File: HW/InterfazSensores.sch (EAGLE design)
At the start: 30 parts, among them IC1 LM2940, T1 BC846, T2 BC846, T3 BC846

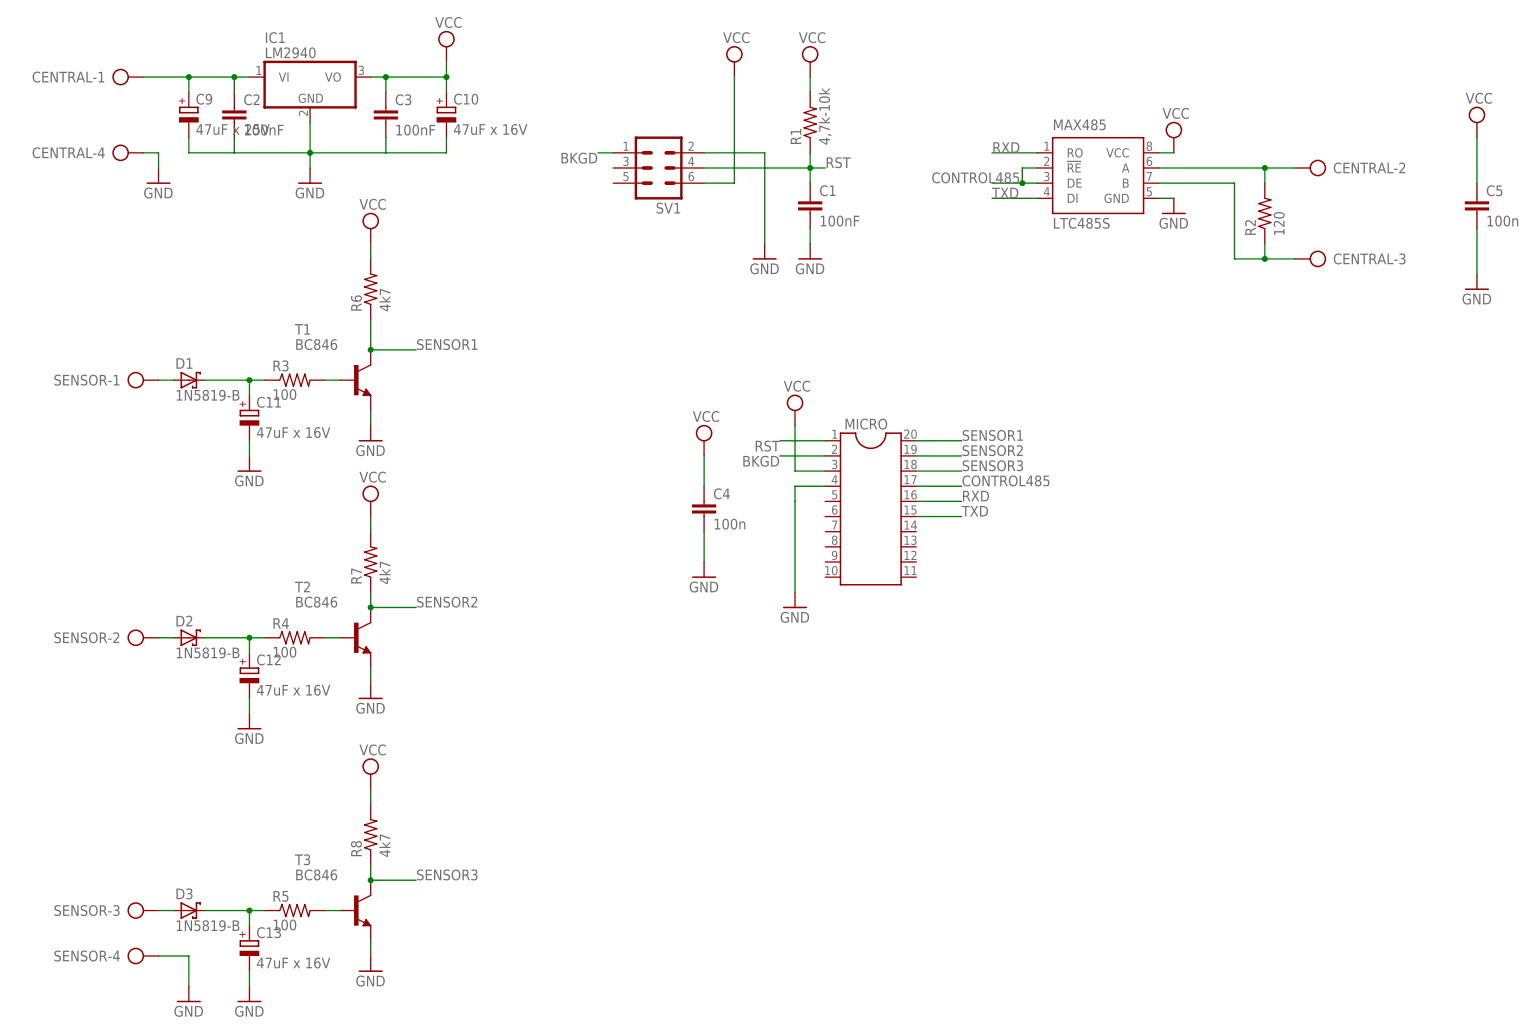
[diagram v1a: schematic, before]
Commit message: Correcciones
Corregimos en placa algunas inconsistencias
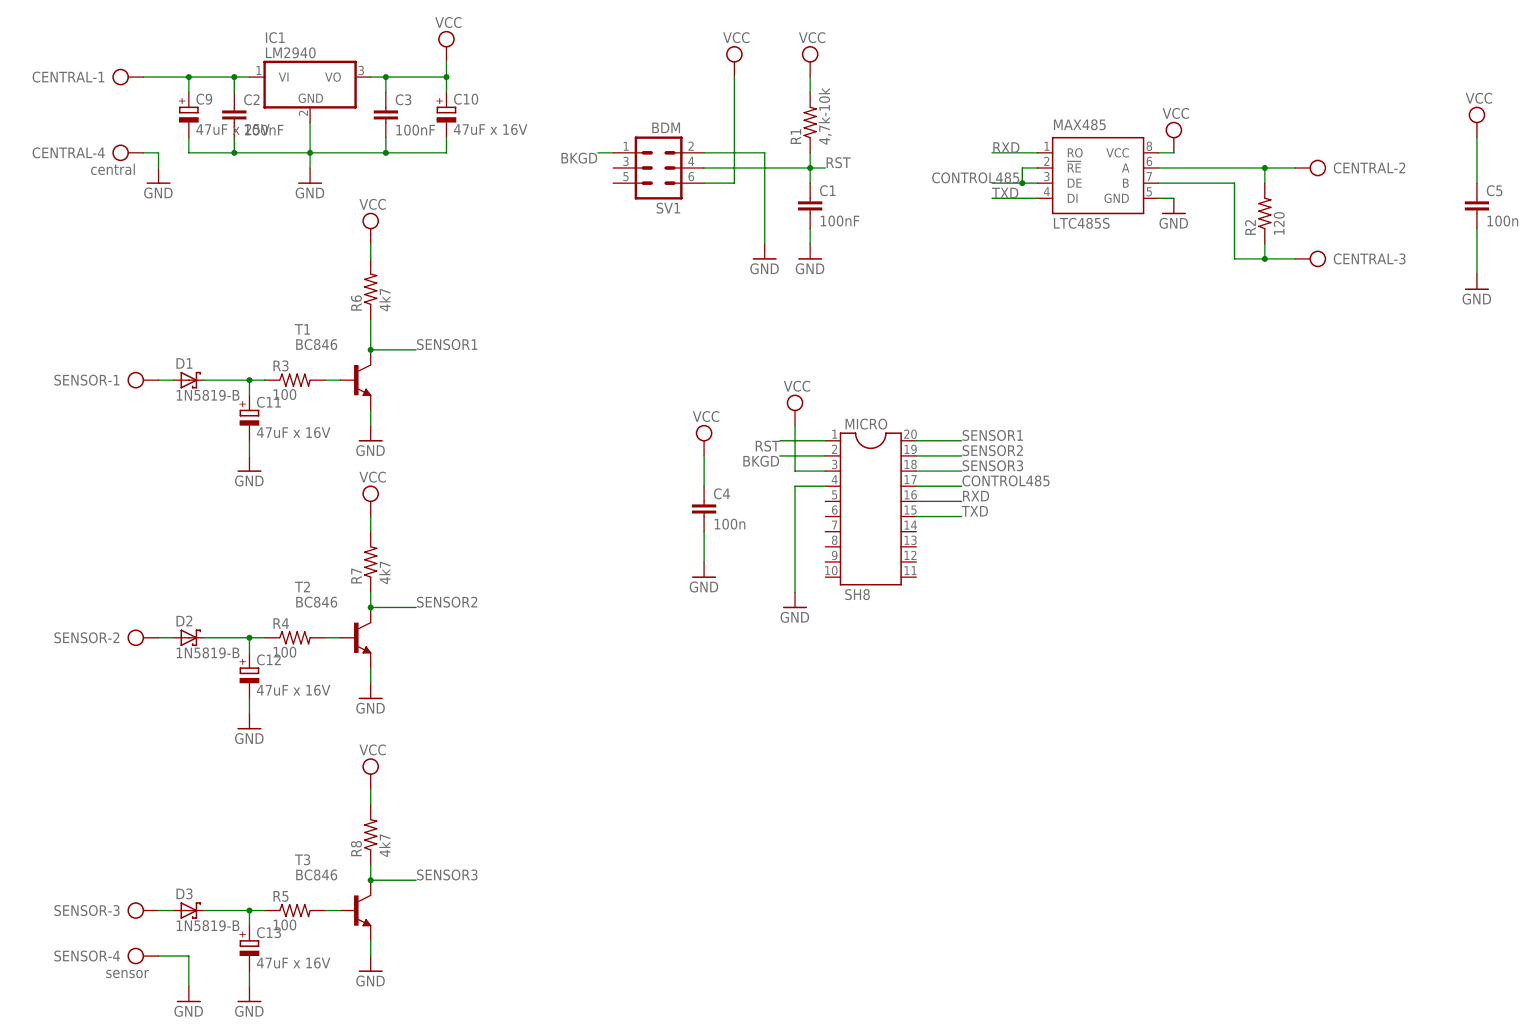
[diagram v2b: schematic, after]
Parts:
- CENTRAL: value (none) -> central
- MICRO: value (none) -> SH8
- SENSOR: value (none) -> sensor
- SV1: value (none) -> BDM
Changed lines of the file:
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@@
 <?xml version="1.0" encoding="utf-8"?>
 <!DOCTYPE eagle SYSTEM "eagle.dtd">
-<eagle version="7.7.0">
+<eagle version="7.6.0">
 <drawing>
 <settings>
@@
 </classes>
 <parts>
-<part name="MICRO" library="ic-package" deviceset="DIL20" device=""/>
+<part name="MICRO" library="ic-package" deviceset="DIL20" device="" value="SH8"/>
 <part name="GND2" library="supply1" deviceset="GND" device=""/>
 <part name="SUPPLY2" library="supply2" deviceset="VCC" device=""/>
@@
 <part name="SUPPLY1" library="supply2" deviceset="VCC" device=""/>
 <part name="GND4" library="supply1" deviceset="GND" device=""/>
-<part name="FRAME1" library="frames" deviceset="A4L-LOC" device=""/>
-<part name="CENTRAL" library="con-ptr500" deviceset="AK300/4" device=""/>
+<part name="FRAME1" library="frames" deviceset="A4L-LOC" device="" value="A4"/>
+<part name="CENTRAL" library="con-ptr500" deviceset="AK300/4" device="" value="central"/>
 <part name="GND1" library="supply1" deviceset="GND" device=""/>
-<part name="SENSOR" library="con-ptr500" deviceset="AK300/4" device=""/>
-<part name="SV1" library="con-lstb" deviceset="MA03-2" device=""/>
+<part name="SENSOR" library="con-ptr500" deviceset="AK300/4" device="" value="sensor"/>
+<part name="SV1" library="con-lstb" deviceset="MA03-2" device="" value="BDM"/>
 <part name="SUPPLY4" library="supply2" deviceset="VCC" device=""/>
 <part name="GND5" library="supply1" deviceset="GND" device=""/>
@@
 <wire x1="-10.16" y1="157.48" x2="-17.78" y2="157.48" width="0.1524" layer="91"/>
 <wire x1="-17.78" y1="157.48" x2="-17.78" y2="160.02" width="0.1524" layer="91"/>
+<junction x="15.24" y="157.48"/>
+<junction x="-10.16" y="157.48"/>
 </segment>
 <segment>
@@
 <pinref part="MICRO" gate="G$1" pin="4"/>
 <wire x1="88.9" y1="101.6" x2="83.82" y2="101.6" width="0.1524" layer="91"/>
-<wire x1="83.82" y1="101.6" x2="83.82" y2="99.06" width="0.1524" layer="91"/>
-<wire x1="83.82" y1="99.06" x2="83.82" y2="83.82" width="0.1524" layer="91"/>
+<wire x1="83.82" y1="101.6" x2="83.82" y2="83.82" width="0.1524" layer="91"/>
 <pinref part="GND8" gate="1" pin="GND"/>
 </segment>
@@
 <net name="SENSOR3" class="0">
 <segment>
-<pinref part="MICRO" gate="G$1" pin="18"/>
-<wire x1="104.14" y1="104.14" x2="111.76" y2="104.14" width="0.1524" layer="91"/>
-<label x="111.76" y="104.14" size="1.778" layer="95"/>
-</segment>
-<segment>
 <pinref part="T3" gate="G$1" pin="C"/>
 <pinref part="R8" gate="G$1" pin="1"/>
@@
 <junction x="12.7" y="35.56"/>
 </segment>
-</net>
+<segment>
+<pinref part="MICRO" gate="G$1" pin="18"/>
+<wire x1="104.14" y1="104.14" x2="111.76" y2="104.14" width="0.1524" layer="91"/>
+<label x="111.76" y="104.14" size="1.778" layer="95"/>
+</segment>
+</net>
